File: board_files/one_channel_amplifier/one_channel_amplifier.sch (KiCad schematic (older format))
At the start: 1 part

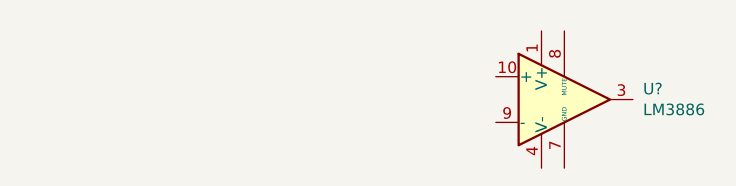
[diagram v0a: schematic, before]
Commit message: added potentiometer to schematic
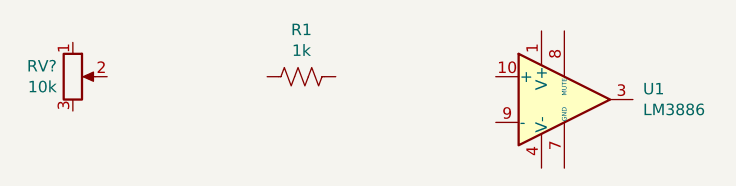
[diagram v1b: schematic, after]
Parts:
- added R1: 1k, Resistor_SMD:R_0805_2012Metric_Pad1.15x1.40mm_HandSolder, symbol Device:R_US
- added RV?: 10k, Potentiometer_THT:Potentiometer_Bourns_3386P_Vertical, symbol Device:R_POT
- U1: renamed from U?; MPN (none) -> LM3886T/NOPB
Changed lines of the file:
@@
 EESchema Schematic File Version 4
+LIBS:one_channel_amplifier-cache
 EELAYER 29 0
 EELAYER END
@@
 $EndDescr
 $Comp
-L Amplifier_Audio:LM3886 U?
+L Amplifier_Audio:LM3886 U1
 U 1 1 5EDEF8D5
 P 4900 3050
-F 0 "U?" H 5244 3096 50  0000 L CNN
+F 0 "U1" H 5244 3096 50  0000 L CNN
 F 1 "LM3886" H 5244 3005 50  0000 L CNN
 F 2 "Package_TO_SOT_THT:TO-220-11_P3.4x5.08mm_StaggerOdd_Lead4.85mm_Vertical" H 4900 3050 50  0001 C CIN
 F 3 "http://www.ti.com/lit/ds/symlink/lm3886.pdf" H 4900 3050 50  0001 C CNN
+F 4 "LM3886T/NOPB" H 4900 3050 50  0001 C CNN "MPN"
 	1    4900 3050
 	1    0    0    -1
 $EndComp
+$Comp
+L Device:R_US R1
+U 1 1 5EDEFF6A
+P 3750 2950
+F 0 "R1" V 3545 2950 50  0000 C CNN
+F 1 "1k" V 3636 2950 50  0000 C CNN
+F 2 "Resistor_SMD:R_0805_2012Metric_Pad1.15x1.40mm_HandSolder" V 3790 2940 50  0001 C CNN
+F 3 "~" H 3750 2950 50  0001 C CNN
+F 4 "RES 1K OHM 1% 1/8W 0805" H 3750 2950 50  0001 C CNN "Description"
+F 5 "CRCW08051K00FKEAC" H 3750 2950 50  0001 C CNN "MPN"
+	1    3750 2950
+	0    1    1    0
+$EndComp
+$Comp
+L Device:R_POT RV?
+U 1 1 5EE0D429
+P 2750 2950
+F 0 "RV?" H 2680 2996 50  0000 R CNN
+F 1 "10k" H 2680 2905 50  0000 R CNN
+F 2 "Potentiometer_THT:Potentiometer_Bourns_3386P_Vertical" H 2750 2950 50  0001 C CNN
+F 3 "~" H 2750 2950 50  0001 C CNN
+F 4 "POT 10K OHM 1/5W PLASTIC LINEAR" H 2750 2950 50  0001 C CNN "Description"
+F 5 "P160KN-0QD15B10K" H 2750 2950 50  0001 C CNN "MPN"
+	1    2750 2950
+	1    0    0    -1
+$EndComp

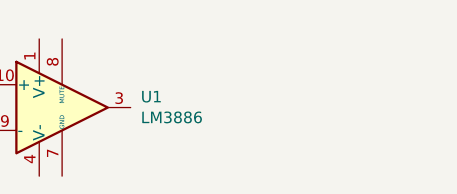
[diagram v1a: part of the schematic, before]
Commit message: added thiele network
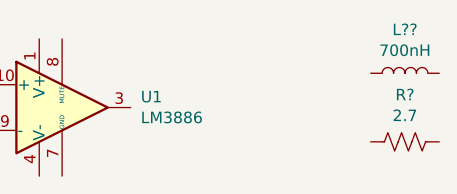
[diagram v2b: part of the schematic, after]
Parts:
- added L??: PA0277NL, Inductor_User:PA0277NL, symbol Inductors_User:PA0277NL
- added R?: 2.7, Resistor_SMD:R_0805_2012Metric_Pad1.15x1.40mm_HandSolder, symbol Device:R_US
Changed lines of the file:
@@
 	1    0    0    -1
 $EndComp
+$Comp
+L Device:R_US R?
+U 1 1 5EE1EFF9
+P 6400 3200
+F 0 "R?" V 6605 3200 50  0000 C CNN
+F 1 "2.7" V 6514 3200 50  0000 C CNN
+F 2 "Resistor_SMD:R_0805_2012Metric_Pad1.15x1.40mm_HandSolder" V 6440 3190 50  0001 C CNN
+F 3 "~" H 6400 3200 50  0001 C CNN
+F 4 "RES 2.7 OHM 1% 1/4W 0805" H 6400 3200 50  0001 C CNN "Description"
+F 5 "RK73H2ATTD2R70F" H 6400 3200 50  0001 C CNN "MPN"
+	1    6400 3200
+	0    -1   -1   0
+$EndComp
+$Comp
+L Inductors_User:PA0277NL L??
+U 1 1 5EE20914
+P 6400 2900
+F 0 "L??" V 6590 2900 50  0000 C CNN
+F 1 "PA0277NL" H 5250 3225 50  0001 C CNN
+F 2 "Inductor_User:PA0277NL" H 5500 3100 50  0001 C CNN
+F 3 "~" H 6400 2900 50  0001 C CNN
+F 4 "FIXED IND 700NH 10.7A 95 MOHM" H 5700 3350 50  0001 C CNN "Description"
+F 5 "700nH" V 6499 2900 50  0000 C CNN "Inductance"
+	1    6400 2900
+	0    -1   -1   0
+$EndComp
 $EndSCHEMATC

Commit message: more schematic progress
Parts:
- added C?: 1500 pF, Capacitor_SMD:C_0805_2012Metric, symbol Device:C
- added C? (x2): 4.7uF, Resistor_SMD:R_1210_3225Metric, symbol Device:C
- added R?: 63.4k, Resistor_SMD:R_0805_2012Metric, symbol Device:R_US
- R1, R?: footprint Resistor_SMD:R_0805_2012Metric_Pad1.15x1.40mm_HandSolder -> Resistor_SMD:R_0805_2012Metric
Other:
- moved on the sheet: R1
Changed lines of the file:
@@
 L Device:R_US R1
 U 1 1 5EDEFF6A
-P 3750 2950
-F 0 "R1" V 3545 2950 50  0000 C CNN
-F 1 "1k" V 3636 2950 50  0000 C CNN
-F 2 "Resistor_SMD:R_0805_2012Metric_Pad1.15x1.40mm_HandSolder" V 3790 2940 50  0001 C CNN
-F 3 "~" H 3750 2950 50  0001 C CNN
-F 4 "RES 1K OHM 1% 1/8W 0805" H 3750 2950 50  0001 C CNN "Description"
-F 5 "CRCW08051K00FKEAC" H 3750 2950 50  0001 C CNN "MPN"
-	1    3750 2950
+P 3250 2950
+F 0 "R1" V 3045 2950 50  0000 C CNN
+F 1 "1k" V 3136 2950 50  0000 C CNN
+F 2 "Resistor_SMD:R_0805_2012Metric" V 3290 2940 50  0001 C CNN
+F 3 "~" H 3250 2950 50  0001 C CNN
+F 4 "RES 1K OHM 1% 1/8W 0805" H 3250 2950 50  0001 C CNN "Description"
+F 5 "CRCW08051K00FKEAC" H 3250 2950 50  0001 C CNN "MPN"
+	1    3250 2950
 	0    1    1    0
 $EndComp
@@
 F 0 "R?" V 6605 3200 50  0000 C CNN
 F 1 "2.7" V 6514 3200 50  0000 C CNN
-F 2 "Resistor_SMD:R_0805_2012Metric_Pad1.15x1.40mm_HandSolder" V 6440 3190 50  0001 C CNN
+F 2 "Resistor_SMD:R_0805_2012Metric" V 6440 3190 50  0001 C CNN
 F 3 "~" H 6400 3200 50  0001 C CNN
 F 4 "RES 2.7 OHM 1% 1/4W 0805" H 6400 3200 50  0001 C CNN "Description"
@@
 	0    -1   -1   0
 $EndComp
+$Comp
+L Device:C C?
+U 1 1 5EE2F0F9
+P 3650 3200
+F 0 "C?" H 3765 3246 50  0000 L CNN
+F 1 "1500 pF" H 3765 3155 50  0000 L CNN
+F 2 "Capacitor_SMD:C_0805_2012Metric" H 3688 3050 50  0001 C CNN
+F 3 "~" H 3650 3200 50  0001 C CNN
+F 4 "CAP CER 1500PF 50V X7R 0805" H 3650 3200 50  0001 C CNN "Description"
+F 5 "885012207087" H 3650 3200 50  0001 C CNN "MPN"
+	1    3650 3200
+	1    0    0    -1
+$EndComp
+$Comp
+L power:GND #PWR?
+U 1 1 5EE300D7
+P 3650 3450
+F 0 "#PWR?" H 3650 3200 50  0001 C CNN
+F 1 "GND" H 3655 3277 50  0000 C CNN
+F 2 "" H 3650 3450 50  0001 C CNN
+F 3 "" H 3650 3450 50  0001 C CNN
+	1    3650 3450
+	1    0    0    -1
+$EndComp
+$Comp
+L Device:R_US R?
+U 1 1 5EE31C96
+P 4900 2400
+F 0 "R?" H 4968 2446 50  0000 L CNN
+F 1 "63.4k" H 4968 2355 50  0000 L CNN
+F 2 "Resistor_SMD:R_0805_2012Metric" V 4940 2390 50  0001 C CNN
+F 3 "~" H 4900 2400 50  0001 C CNN
+F 4 "RES SMD 63.4K OHM 1% 1/8W 0805" H 4900 2400 50  0001 C CNN "Description"
+F 5 "ERJ-6ENF6342V" H 4900 2400 50  0001 C CNN "MPN"
+	1    4900 2400
+	1    0    0    -1
+$EndComp
+$Comp
+L Device:C C?
+U 1 1 5EE32C87
+P 2750 1150
+F 0 "C?" H 2865 1196 50  0000 L CNN
+F 1 "4.7uF" H 2865 1105 50  0000 L CNN
+F 2 "Resistor_SMD:R_1210_3225Metric" H 2788 1000 50  0001 C CNN
+F 3 "~" H 2750 1150 50  0001 C CNN
+F 4 "CAP CER 4.7UF 100V X7R 1210" H 2750 1150 50  0001 C CNN "Description"
+F 5 "CL32B475KCVZW6E" H 2750 1150 50  0001 C CNN "MPN"
+	1    2750 1150
+	1    0    0    -1
+$EndComp
+$Comp
+L Device:C C?
+U 1 1 5EE34F85
+P 2750 1800
+F 0 "C?" H 2865 1846 50  0000 L CNN
+F 1 "4.7uF" H 2865 1755 50  0000 L CNN
+F 2 "Resistor_SMD:R_1210_3225Metric" H 2788 1650 50  0001 C CNN
+F 3 "~" H 2750 1800 50  0001 C CNN
+F 4 "CAP CER 4.7UF 100V X7R 1210" H 2750 1800 50  0001 C CNN "Description"
+F 5 "CL32B475KCVZW6E" H 2750 1800 50  0001 C CNN "MPN"
+	1    2750 1800
+	1    0    0    -1
+$EndComp
 $EndSCHEMATC

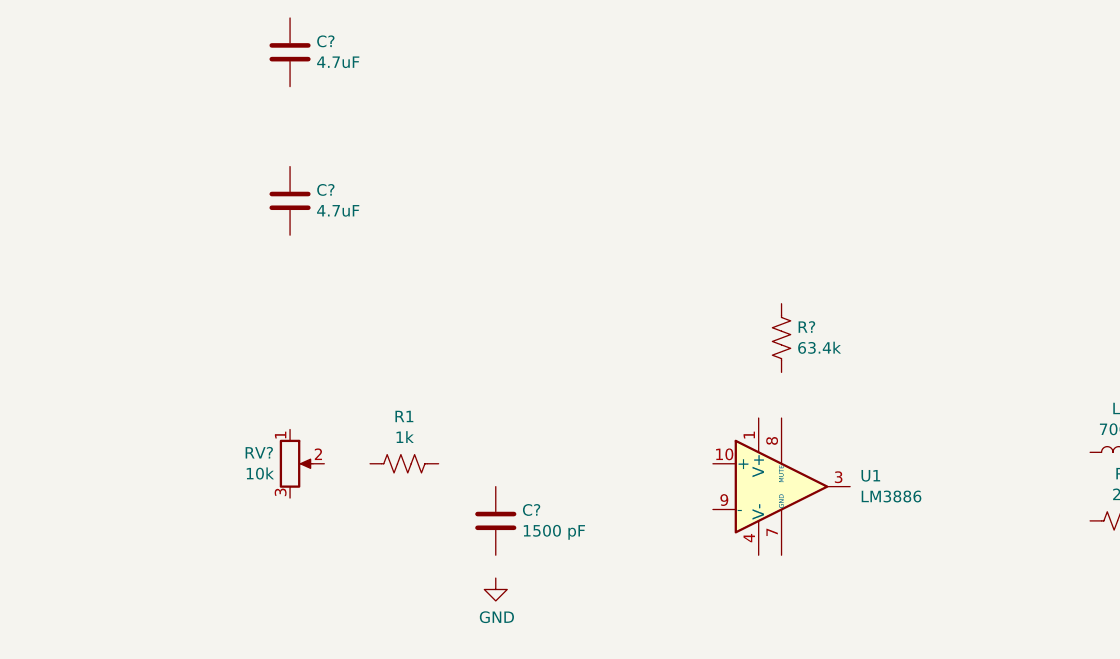
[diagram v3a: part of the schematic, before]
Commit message: finished bypass caps
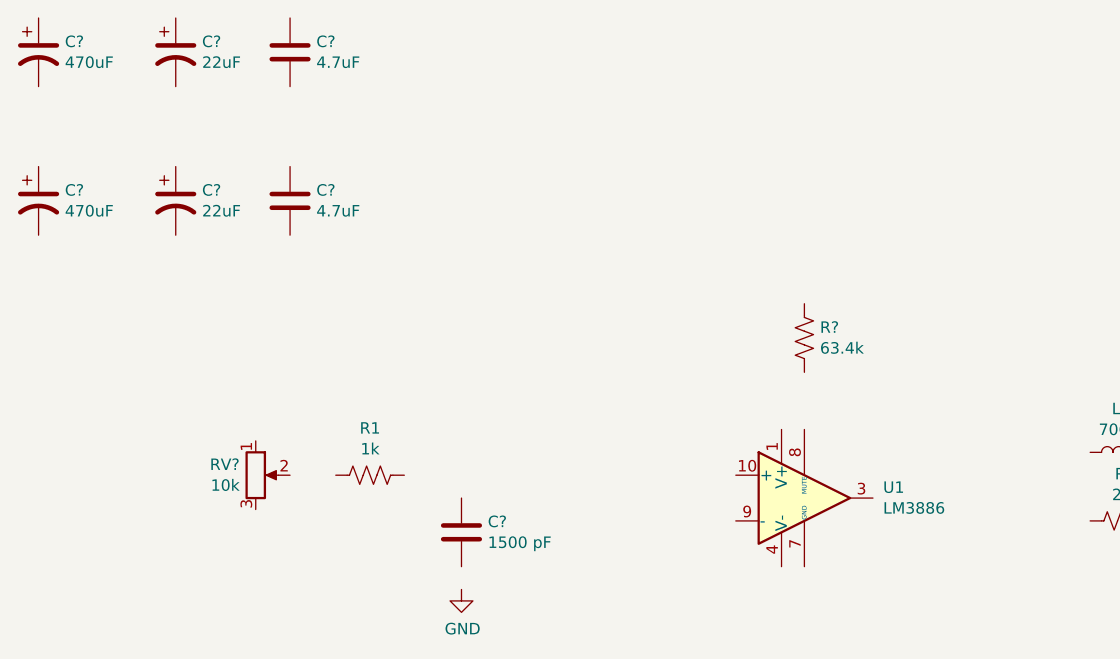
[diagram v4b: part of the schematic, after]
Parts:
- added C? (x2): 470uF, Capacitor_THT:CP_Radial_D16.0mm_P7.50mm, symbol Device:CP1
- added C? (x2): 22uF, Capacitor_THT:CP_Radial_D10.0mm_P5.00mm, symbol Device:CP1
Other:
- moved on the sheet: C?, R1, R?, RV?, U1
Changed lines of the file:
@@
 L Amplifier_Audio:LM3886 U1
 U 1 1 5EDEF8D5
-P 4900 3050
-F 0 "U1" H 5244 3096 50  0000 L CNN
-F 1 "LM3886" H 5244 3005 50  0000 L CNN
-F 2 "Package_TO_SOT_THT:TO-220-11_P3.4x5.08mm_StaggerOdd_Lead4.85mm_Vertical" H 4900 3050 50  0001 C CIN
-F 3 "http://www.ti.com/lit/ds/symlink/lm3886.pdf" H 4900 3050 50  0001 C CNN
-F 4 "LM3886T/NOPB" H 4900 3050 50  0001 C CNN "MPN"
-	1    4900 3050
+P 5000 3100
+F 0 "U1" H 5344 3146 50  0000 L CNN
+F 1 "LM3886" H 5344 3055 50  0000 L CNN
+F 2 "Package_TO_SOT_THT:TO-220-11_P3.4x5.08mm_StaggerOdd_Lead4.85mm_Vertical" H 5000 3100 50  0001 C CIN
+F 3 "http://www.ti.com/lit/ds/symlink/lm3886.pdf" H 5000 3100 50  0001 C CNN
+F 4 "LM3886T/NOPB" H 5000 3100 50  0001 C CNN "MPN"
+	1    5000 3100
 	1    0    0    -1
 $EndComp
@@
 L Device:R_US R1
 U 1 1 5EDEFF6A
-P 3250 2950
-F 0 "R1" V 3045 2950 50  0000 C CNN
-F 1 "1k" V 3136 2950 50  0000 C CNN
-F 2 "Resistor_SMD:R_0805_2012Metric" V 3290 2940 50  0001 C CNN
-F 3 "~" H 3250 2950 50  0001 C CNN
-F 4 "RES 1K OHM 1% 1/8W 0805" H 3250 2950 50  0001 C CNN "Description"
-F 5 "CRCW08051K00FKEAC" H 3250 2950 50  0001 C CNN "MPN"
-	1    3250 2950
+P 3100 3000
+F 0 "R1" V 2895 3000 50  0000 C CNN
+F 1 "1k" V 2986 3000 50  0000 C CNN
+F 2 "Resistor_SMD:R_0805_2012Metric" V 3140 2990 50  0001 C CNN
+F 3 "~" H 3100 3000 50  0001 C CNN
+F 4 "RES 1K OHM 1% 1/8W 0805" H 3100 3000 50  0001 C CNN "Description"
+F 5 "CRCW08051K00FKEAC" H 3100 3000 50  0001 C CNN "MPN"
+	1    3100 3000
 	0    1    1    0
 $EndComp
@@
 L Device:R_POT RV?
 U 1 1 5EE0D429
-P 2750 2950
-F 0 "RV?" H 2680 2996 50  0000 R CNN
-F 1 "10k" H 2680 2905 50  0000 R CNN
-F 2 "Potentiometer_THT:Potentiometer_Bourns_3386P_Vertical" H 2750 2950 50  0001 C CNN
-F 3 "~" H 2750 2950 50  0001 C CNN
-F 4 "POT 10K OHM 1/5W PLASTIC LINEAR" H 2750 2950 50  0001 C CNN "Description"
-F 5 "P160KN-0QD15B10K" H 2750 2950 50  0001 C CNN "MPN"
-	1    2750 2950
+P 2600 3000
+F 0 "RV?" H 2530 3046 50  0000 R CNN
+F 1 "10k" H 2530 2955 50  0000 R CNN
+F 2 "Potentiometer_THT:Potentiometer_Bourns_3386P_Vertical" H 2600 3000 50  0001 C CNN
+F 3 "~" H 2600 3000 50  0001 C CNN
+F 4 "POT 10K OHM 1/5W PLASTIC LINEAR" H 2600 3000 50  0001 C CNN "Description"
+F 5 "P160KN-0QD15B10K" H 2600 3000 50  0001 C CNN "MPN"
+	1    2600 3000
 	1    0    0    -1
 $EndComp
@@
 L Device:C C?
 U 1 1 5EE2F0F9
-P 3650 3200
-F 0 "C?" H 3765 3246 50  0000 L CNN
-F 1 "1500 pF" H 3765 3155 50  0000 L CNN
-F 2 "Capacitor_SMD:C_0805_2012Metric" H 3688 3050 50  0001 C CNN
-F 3 "~" H 3650 3200 50  0001 C CNN
-F 4 "CAP CER 1500PF 50V X7R 0805" H 3650 3200 50  0001 C CNN "Description"
-F 5 "885012207087" H 3650 3200 50  0001 C CNN "MPN"
-	1    3650 3200
+P 3500 3250
+F 0 "C?" H 3615 3296 50  0000 L CNN
+F 1 "1500 pF" H 3615 3205 50  0000 L CNN
+F 2 "Capacitor_SMD:C_0805_2012Metric" H 3538 3100 50  0001 C CNN
+F 3 "~" H 3500 3250 50  0001 C CNN
+F 4 "CAP CER 1500PF 50V X7R 0805" H 3500 3250 50  0001 C CNN "Description"
+F 5 "885012207087" H 3500 3250 50  0001 C CNN "MPN"
+	1    3500 3250
 	1    0    0    -1
 $EndComp
@@
 L power:GND #PWR?
 U 1 1 5EE300D7
-P 3650 3450
-F 0 "#PWR?" H 3650 3200 50  0001 C CNN
-F 1 "GND" H 3655 3277 50  0000 C CNN
-F 2 "" H 3650 3450 50  0001 C CNN
-F 3 "" H 3650 3450 50  0001 C CNN
-	1    3650 3450
+P 3500 3500
+F 0 "#PWR?" H 3500 3250 50  0001 C CNN
+F 1 "GND" H 3505 3327 50  0000 C CNN
+F 2 "" H 3500 3500 50  0001 C CNN
+F 3 "" H 3500 3500 50  0001 C CNN
+	1    3500 3500
 	1    0    0    -1
 $EndComp
@@
 L Device:R_US R?
 U 1 1 5EE31C96
-P 4900 2400
-F 0 "R?" H 4968 2446 50  0000 L CNN
-F 1 "63.4k" H 4968 2355 50  0000 L CNN
-F 2 "Resistor_SMD:R_0805_2012Metric" V 4940 2390 50  0001 C CNN
-F 3 "~" H 4900 2400 50  0001 C CNN
-F 4 "RES SMD 63.4K OHM 1% 1/8W 0805" H 4900 2400 50  0001 C CNN "Description"
-F 5 "ERJ-6ENF6342V" H 4900 2400 50  0001 C CNN "MPN"
-	1    4900 2400
+P 5000 2400
+F 0 "R?" H 5068 2446 50  0000 L CNN
+F 1 "63.4k" H 5068 2355 50  0000 L CNN
+F 2 "Resistor_SMD:R_0805_2012Metric" V 5040 2390 50  0001 C CNN
+F 3 "~" H 5000 2400 50  0001 C CNN
+F 4 "RES SMD 63.4K OHM 1% 1/8W 0805" H 5000 2400 50  0001 C CNN "Description"
+F 5 "ERJ-6ENF6342V" H 5000 2400 50  0001 C CNN "MPN"
+	1    5000 2400
 	1    0    0    -1
 $EndComp
@@
 	1    0    0    -1
 $EndComp
+$Comp
+L Device:CP1 C?
+U 1 1 5EE45CE1
+P 1650 1150
+F 0 "C?" H 1765 1196 50  0000 L CNN
+F 1 "470uF" H 1765 1105 50  0000 L CNN
+F 2 "Capacitor_THT:CP_Radial_D16.0mm_P7.50mm" H 1650 1150 50  0001 C CNN
+F 3 "~" H 1650 1150 50  0001 C CNN
+F 4 "CAP ALUM 470UF 20% 100V RADIAL" H 1650 1150 50  0001 C CNN "Description"
+F 5 "ECA-2AHG471B" H 1650 1150 50  0001 C CNN "MPN"
+	1    1650 1150
+	1    0    0    -1
+$EndComp
+$Comp
+L Device:CP1 C?
+U 1 1 5EE47E8E
+P 1650 1800
+F 0 "C?" H 1765 1846 50  0000 L CNN
+F 1 "470uF" H 1765 1755 50  0000 L CNN
+F 2 "Capacitor_THT:CP_Radial_D16.0mm_P7.50mm" H 1650 1800 50  0001 C CNN
+F 3 "~" H 1650 1800 50  0001 C CNN
+F 4 "CAP ALUM 470UF 20% 100V RADIAL" H 1650 1800 50  0001 C CNN "Description"
+F 5 "ECA-2AHG471B" H 1650 1800 50  0001 C CNN "MPN"
+	1    1650 1800
+	1    0    0    -1
+$EndComp
+$Comp
+L Device:CP1 C?
+U 1 1 5EE4803C
+P 2250 1150
+F 0 "C?" H 2365 1196 50  0000 L CNN
+F 1 "22uF" H 2365 1105 50  0000 L CNN
+F 2 "Capacitor_THT:CP_Radial_D10.0mm_P5.00mm" H 2250 1150 50  0001 C CNN
+F 3 "~" H 2250 1150 50  0001 C CNN
+F 4 "CAP ALUM POLY 22UF 20% 100V T/H" H 2250 1150 50  0001 C CNN "Description"
+F 5 "100SXE22M" H 2250 1150 50  0001 C CNN "MPN"
+	1    2250 1150
+	1    0    0    -1
+$EndComp
+$Comp
+L Device:CP1 C?
+U 1 1 5EE4A479
+P 2250 1800
+F 0 "C?" H 2365 1846 50  0000 L CNN
+F 1 "22uF" H 2365 1755 50  0000 L CNN
+F 2 "Capacitor_THT:CP_Radial_D10.0mm_P5.00mm" H 2250 1800 50  0001 C CNN
+F 3 "~" H 2250 1800 50  0001 C CNN
+F 4 "CAP ALUM POLY 22UF 20% 100V T/H" H 2250 1800 50  0001 C CNN "Description"
+F 5 "100SXE22M" H 2250 1800 50  0001 C CNN "MPN"
+	1    2250 1800
+	1    0    0    -1
+$EndComp

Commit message: finished adding components
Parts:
- removed C?: 1500 pF, Capacitor_SMD:C_0805_2012Metric, symbol Device:C
- added C?: 1500pF, Capacitor_SMD:C_0805_2012Metric, symbol Device:C_Small
- added C? (x2): 0.1uF, Capacitor_SMD:C_0603_1608Metric, symbol Device:C_Small
- added C?: CP1_Small, symbol Device:CP1_Small
- added C?: 51pF, Capacitor_SMD:C_0603_1608Metric, symbol Device:C_Small
- added C?: 220pF, Capacitor_SMD:C_0805_2012Metric, symbol Device:C_Small
- added R?: 100k, Resistor_SMD:R_0805_2012Metric, symbol Device:R_US
- added R?: 6.34k, Capacitor_SMD:C_0805_2012Metric, symbol Device:R_US
- added R?: 20k, Resistor_SMD:R_0603_1608Metric, symbol Device:R_US
- added R?: 2.7, Resistor_SMD:R_0805_2012Metric, symbol Device:R_US
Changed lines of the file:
@@
-$EndComp
-$Comp
-L Device:C C?
-U 1 1 5EE2F0F9
-P 3500 3250
-F 0 "C?" H 3615 3296 50  0000 L CNN
-F 1 "1500 pF" H 3615 3205 50  0000 L CNN
-F 2 "Capacitor_SMD:C_0805_2012Metric" H 3538 3100 50  0001 C CNN
-F 3 "~" H 3500 3250 50  0001 C CNN
-F 4 "CAP CER 1500PF 50V X7R 0805" H 3500 3250 50  0001 C CNN "Description"
-F 5 "885012207087" H 3500 3250 50  0001 C CNN "MPN"
-	1    3500 3250
-	1    0    0    -1
 $EndComp
 $Comp
@@
 	1    0    0    -1
 $EndComp
+$Comp
+L Device:C_Small C?
+U 1 1 5EE43F34
+P 3500 3200
+F 0 "C?" H 3592 3246 50  0000 L CNN
+F 1 "1500pF" H 3592 3155 50  0000 L CNN
+F 2 "Capacitor_SMD:C_0805_2012Metric" H 3500 3200 50  0001 C CNN
+F 3 "~" H 3500 3200 50  0001 C CNN
+F 4 "885012207087" H 3500 3200 50  0001 C CNN "MPN"
+F 5 "CAP CER 1500PF 50V X7R 0805" H 3500 3200 50  0001 C CNN "Description"
+	1    3500 3200
+	1    0    0    -1
+$EndComp
+$Comp
+L Device:C_Small C?
+U 1 1 5EE47520
+P 5800 5600
+F 0 "C?" H 5892 5646 50  0000 L CNN
+F 1 "0.1uF" H 5892 5555 50  0000 L CNN
+F 2 "Capacitor_SMD:C_0603_1608Metric" H 5800 5600 50  0001 C CNN
+F 3 "~" H 5800 5600 50  0001 C CNN
+F 4 "CAP CER 0.1UF 100V X7R 0603" H 5800 5600 50  0001 C CNN "Description"
+F 5 "CC0603KRX7R0BB104" H 5800 5600 50  0001 C CNN "MPN"
+	1    5800 5600
+	1    0    0    -1
+$EndComp
+$Comp
+L Device:CP1_Small C?
+U 1 1 5EE4802C
+P 5550 2350
+F 0 "C?" H 5641 2396 50  0000 L CNN
+F 1 "CP1_Small" H 5641 2305 50  0000 L CNN
+F 2 "" H 5550 2350 50  0001 C CNN
+F 3 "~" H 5550 2350 50  0001 C CNN
+	1    5550 2350
+	1    0    0    -1
+$EndComp
+$Comp
+L Device:R_US R?
+U 1 1 5EE48FF4
+P 5000 4450
+F 0 "R?" V 4795 4450 50  0000 C CNN
+F 1 "100k" V 4886 4450 50  0000 C CNN
+F 2 "Resistor_SMD:R_0805_2012Metric" V 5040 4440 50  0001 C CNN
+F 3 "~" H 5000 4450 50  0001 C CNN
+F 4 "RES SMD 100K OHM 1% 1/8W 0805" H 5000 4450 50  0001 C CNN "Description"
+F 5 "RC0805FR-07100KL" H 5000 4450 50  0001 C CNN "MPN"
+	1    5000 4450
+	0    1    1    0
+$EndComp
+$Comp
+L Device:R_US R?
+U 1 1 5EE4A847
+P 4150 5200
+F 0 "R?" H 4218 5246 50  0000 L CNN
+F 1 "6.34k" H 4218 5155 50  0000 L CNN
+F 2 "Capacitor_SMD:C_0805_2012Metric" V 4190 5190 50  0001 C CNN
+F 3 "~" H 4150 5200 50  0001 C CNN
+F 4 "RES SMD 6.34K OHM 1% 1/8W 0805" H 4150 5200 50  0001 C CNN "Description"
+F 5 "ERJ-6ENF6341V" H 4150 5200 50  0001 C CNN "MPN"
+	1    4150 5200
+	1    0    0    -1
+$EndComp
+$Comp
+L Device:R_US R?
+U 1 1 5EE4BBD5
+P 5350 4950
+F 0 "R?" V 5145 4950 50  0000 C CNN
+F 1 "20k" V 5236 4950 50  0000 C CNN
+F 2 "Resistor_SMD:R_0603_1608Metric" V 5390 4940 50  0001 C CNN
+F 3 "~" H 5350 4950 50  0001 C CNN
+F 4 "RES SMD 20K OHM 1% 1/10W 0603" H 5350 4950 50  0001 C CNN "Description"
+F 5 "ERJ-3EKF2002V" H 5350 4950 50  0001 C CNN "MPN"
+	1    5350 4950
+	0    1    1    0
+$EndComp
+$Comp
+L Device:C_Small C?
+U 1 1 5EE4E1EF
+P 4750 4950
+F 0 "C?" V 4979 4950 50  0000 C CNN
+F 1 "51pF" V 4888 4950 50  0000 C CNN
+F 2 "Capacitor_SMD:C_0603_1608Metric" H 4750 4950 50  0001 C CNN
+F 3 "~" H 4750 4950 50  0001 C CNN
+F 4 "CAP CER 51PF 50V C0G/NP0 0603" H 4750 4950 50  0001 C CNN "Description"
+F 5 "CL10C510JB8NNNC" H 4750 4950 50  0001 C CNN "MPN"
+	1    4750 4950
+	0    -1   -1   0
+$EndComp
+$Comp
+L Device:C_Small C?
+U 1 1 5EE5C5F8
+P 4300 3100
+F 0 "C?" H 4208 3054 50  0000 R CNN
+F 1 "220pF" H 4208 3145 50  0000 R CNN
+F 2 "Capacitor_SMD:C_0805_2012Metric" H 4300 3100 50  0001 C CNN
+F 3 "~" H 4300 3100 50  0001 C CNN
+F 4 "CAP CER 220PF 10V X7R 0805" H 4300 3100 50  0001 C CNN "Description"
+F 5 "885012207005" H 4300 3100 50  0001 C CNN "MPN"
+	1    4300 3100
+	-1   0    0    1
+$EndComp
+$Comp
+L Device:C_Small C?
+U 1 1 5EE5EB47
+P 4150 5600
+F 0 "C?" H 4242 5646 50  0000 L CNN
+F 1 "0.1uF" H 4242 5555 50  0000 L CNN
+F 2 "Capacitor_SMD:C_0603_1608Metric" H 4150 5600 50  0001 C CNN
+F 3 "~" H 4150 5600 50  0001 C CNN
+F 4 "CAP CER 0.1UF 100V X7R 0603" H 4150 5600 50  0001 C CNN "Description"
+F 5 "CC0603KRX7R0BB104" H 4150 5600 50  0001 C CNN "MPN"
+	1    4150 5600
+	1    0    0    -1
+$EndComp
+$Comp
+L Device:R_US R?
+U 1 1 5EE60B0A
+P 5800 5200
+F 0 "R?" V 6005 5200 50  0000 C CNN
+F 1 "2.7" V 5914 5200 50  0000 C CNN
+F 2 "Resistor_SMD:R_0805_2012Metric" V 5840 5190 50  0001 C CNN
+F 3 "~" H 5800 5200 50  0001 C CNN
+F 4 "RES 2.7 OHM 1% 1/4W 0805" H 5800 5200 50  0001 C CNN "Description"
+F 5 "RK73H2ATTD2R70F" H 5800 5200 50  0001 C CNN "MPN"
+	1    5800 5200
+	1    0    0    -1
+$EndComp
